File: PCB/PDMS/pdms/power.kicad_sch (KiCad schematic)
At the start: 42 parts, among them IC1 BD50FD0WHFP-TR, IC10 LDO40LPU50RY, IC11 MP2332HGTL-P, IC14 LDO40LPU50RY, IC3 LDO40LPU33RY, Q1 AO3401A, Q11 AO3401A

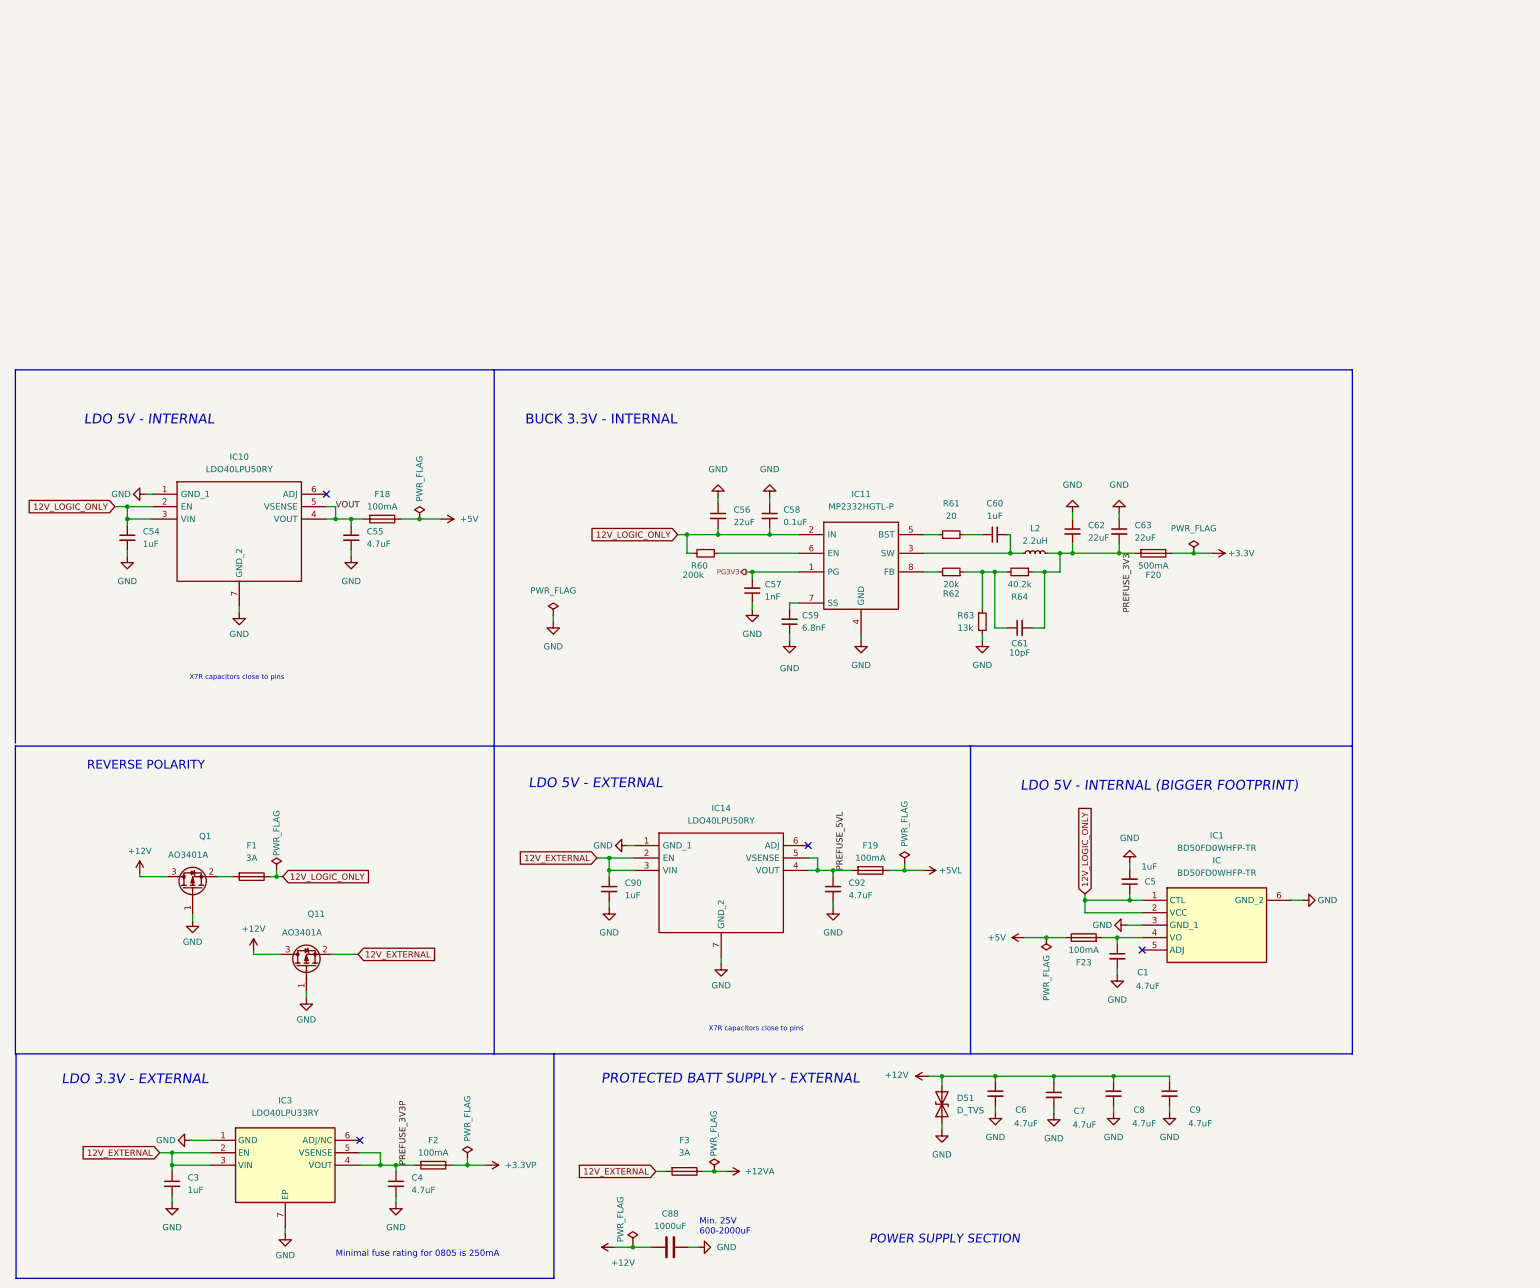
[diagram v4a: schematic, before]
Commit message: FINISHED: Version with fusing and input power filtering
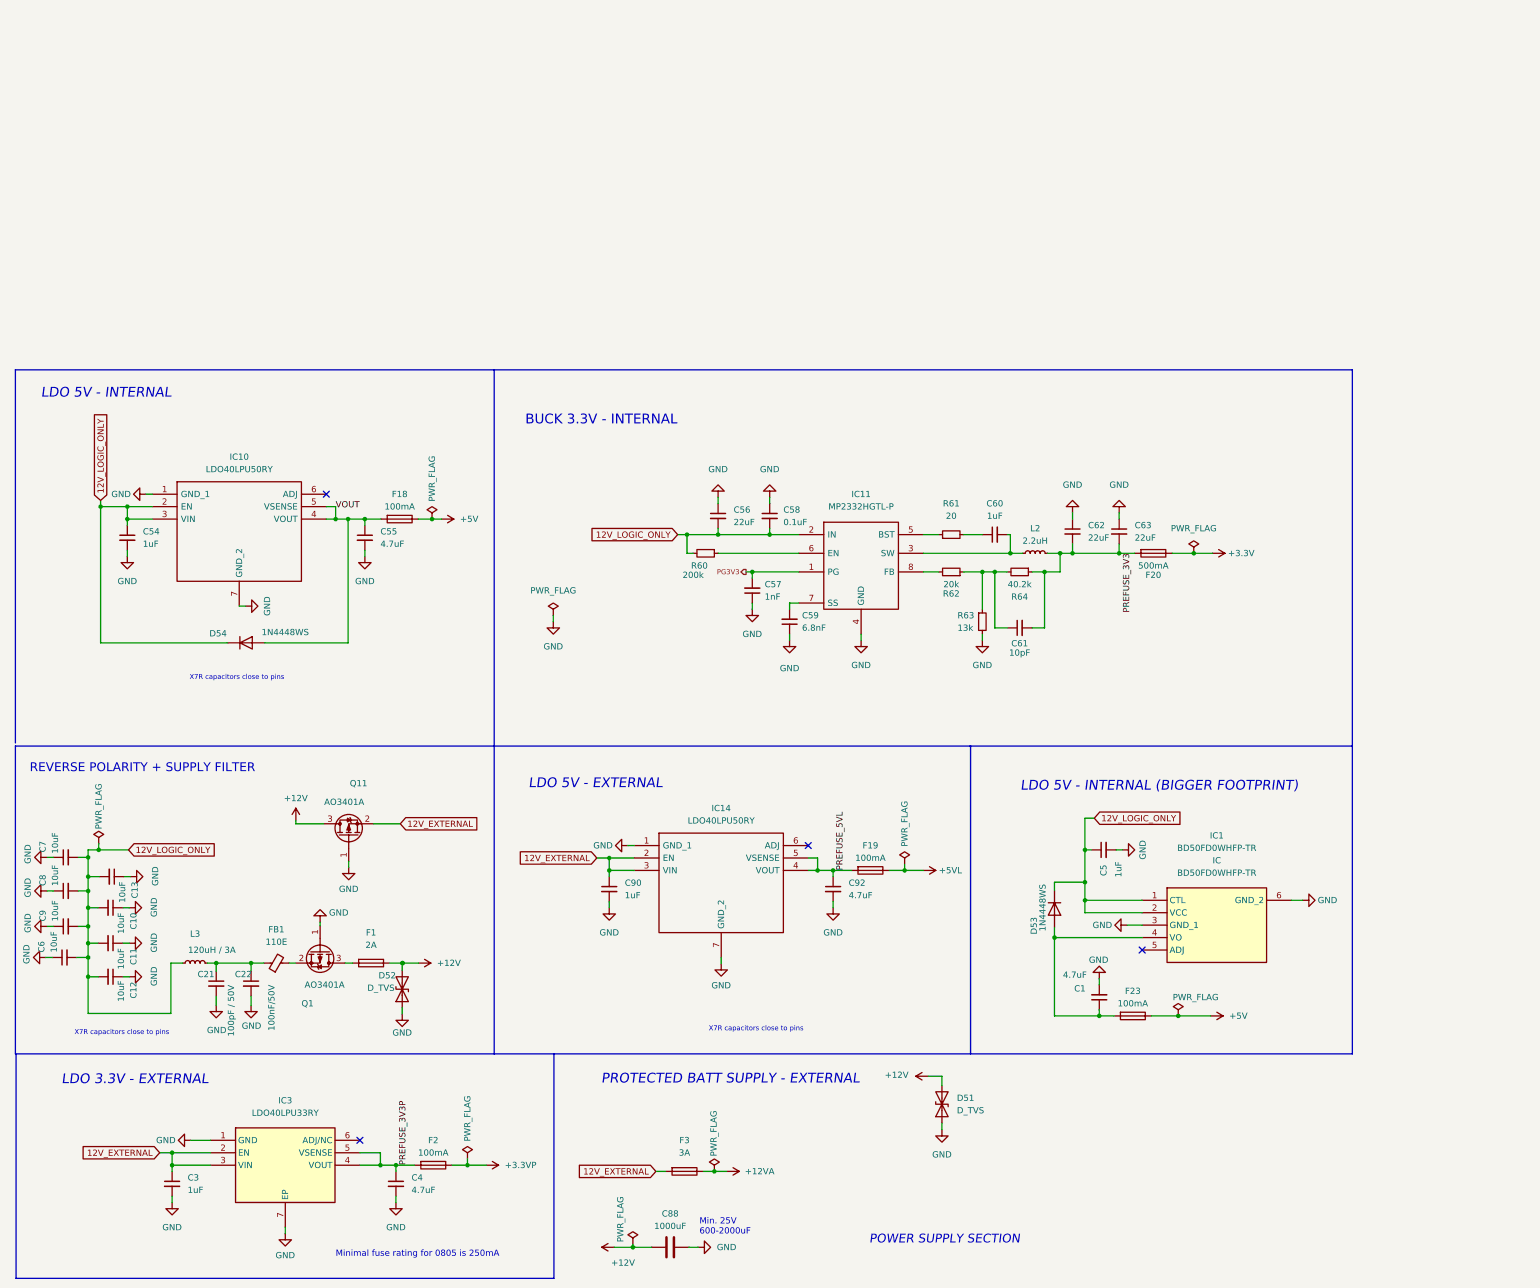
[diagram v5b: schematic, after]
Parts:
- added C10, C11, C12, C13: 10uF, Capacitor_SMD:C_1206_3216Metric, symbol Device:C_Small
- added C21: 100pF / 50V, Capacitor_SMD:C_0402_1005Metric, symbol Device:C_Small
- added C22: 100nF/50V, Capacitor_SMD:C_0402_1005Metric, symbol Device:C_Small
- added D52: D_TVS, Diode_SMD:D_SMC, symbol Device:D_TVS
- added D53, D54: 1N4448WS, Diode_SMD:D_SOD-323, symbol Diode:1N4448WS
- added FB1: 110E, Inductor_SMD:L_1206_3216Metric, symbol Device:FerriteBead_Small
- added L3: 120uH / 3A, Inductor_SMD:L_6.3x6.3_H3, symbol Device:L_Small
- C6, C7, C8, C9: value 4.7uF -> 10uF
- F1: value 3A -> 2A; footprint Fuse:Fuse_0805_2012Metric -> Fuse:Fuse_1206_3216Metric
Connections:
- net +12V: now also F1.1, D52.2 (A2); no longer C6.1, C7.1, C8.1, C9.1, Q1.3 (D)
- net 12V_LOGIC_ONLY: now also C6.2, C7.2, C8.2, C9.2, C10.2, C11.2, C12.2, C13.2, D53.1 (K), D54.1 (K), L3.1; no longer F1.1
- net GND: now also C6.1, C7.1, C8.1, C9.1, C10.1, C11.1, C12.1, C13.1, C21.2, C22.2, D52.1 (A1); no longer C6.2, C7.2, C8.2, C9.2
- net VOUT: now also D54.2 (A)
- net at C1.1, F23.2, IC1.4 (VO): now also D53.2 (A)
- net at Q1.2 (S): now also FB1.2; no longer F1.2
- new net: C21.1, C22.1, FB1.1, L3.2
- new net: F1.2, Q1.3 (D)
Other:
- note added: "REVERSE POLARITY + SUPPLY FILTER"
- note removed: "REVERSE POLARITY"
- moved on the sheet: C1, C5, C55, F1, F18, F23, Q1, Q11

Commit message: Ver 4.2 ready + BTS50025 test board
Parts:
- added C23, C24: 4.7uF, Capacitor_SMD:C_1206_3216Metric, symbol Device:C_Small
- added C25, C26: 0.1uF, Capacitor_SMD:C_0805_2012Metric, symbol Device:C_Small
- added C27: 1uF, Resistor_SMD:R_0402_1005Metric, symbol Device:C_Small
- added C28: 47nF, Resistor_SMD:R_0402_1005Metric, symbol Device:C_Small
- added C29: 10pF, Resistor_SMD:R_0402_1005Metric, symbol Device:C_Small
- added C30, C31: 22uF, Capacitor_SMD:C_1206_3216Metric, symbol Device:C_Small
- added F24: 500mA, Fuse:Fuse_0805_2012Metric, symbol Device:Fuse
- added L4: 2.2uH, Inductor_SMD:L_Vishay_IHLP-1616, symbol Device:L_Small
- added R120: 15k, Resistor_SMD:R_0402_1005Metric, symbol Device:R_Small
- added R121, R122, R124: 100k, Resistor_SMD:R_0402_1005Metric, symbol Device:R_Small
- added R123: 31.6k, Resistor_SMD:R_0402_1005Metric, symbol Device:R_Small
- added U7: MP4322GDE-P, PDMS_Additional:QFN-12_MP4322_MNP, symbol pdms_additional:MP4322GDE-P
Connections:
- net +3.3V: now also F24.1
- net 12V_LOGIC_ONLY: now also C23.1, C24.1, C25.1, C26.1, R121.1, U7.10 (VIN), U7.2 (VIN)
- net GND: now also C23.2, C24.2, C25.2, C26.2, C27.2, C30.2, C31.2, R120.1, R123.2, U7.1 (PGND), U7.11 (PGND), U7.6 (AGND)
- net PREFUSE_3V3: now also C29.2, C30.1, C31.1, F24.2, L4.2, R124.1
- new net: C29.1, R123.1, R124.2, U7.7 (FB)
- new net: R121.2, U7.9 (EN)
- new net: C28.2, L4.1, U7.12 (SW)
- new net: C28.1, U7.3 (BOOT)
- new net: R120.2, U7.4 (FREQ)
- new net: C27.1, R122.1, U7.5 (VCC)
- new net: R122.2, U7.8 (PG)
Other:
- note added: "(1206)"

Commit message: Minor changes in overall schematics & MP4322 scheamtics
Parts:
- removed C23, C24: 4.7uF, Capacitor_SMD:C_1206_3216Metric, symbol Device:C_Small
- removed C25, C26: 0.1uF, Capacitor_SMD:C_0805_2012Metric, symbol Device:C_Small
- removed C27: 1uF, Resistor_SMD:R_0402_1005Metric, symbol Device:C_Small
- removed C28: 47nF, Resistor_SMD:R_0402_1005Metric, symbol Device:C_Small
- removed C29: 10pF, Resistor_SMD:R_0402_1005Metric, symbol Device:C_Small
- removed C30, C31: 22uF, Capacitor_SMD:C_1206_3216Metric, symbol Device:C_Small
- removed F24: 500mA, Fuse:Fuse_0805_2012Metric, symbol Device:Fuse
- removed L4: 2.2uH, Inductor_SMD:L_Vishay_IHLP-1616, symbol Device:L_Small
- removed R120: 15k, Resistor_SMD:R_0402_1005Metric, symbol Device:R_Small
- removed R121, R122, R124: 100k, Resistor_SMD:R_0402_1005Metric, symbol Device:R_Small
- removed R123: 31.6k, Resistor_SMD:R_0402_1005Metric, symbol Device:R_Small
- removed U7: MP4322GDE-P, PDMS_Additional:QFN-12_MP4322_MNP, symbol pdms_additional:MP4322GDE-P
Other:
- added sheet mp4322 (mp4322.kicad_sch)
- note removed: "(1206)"

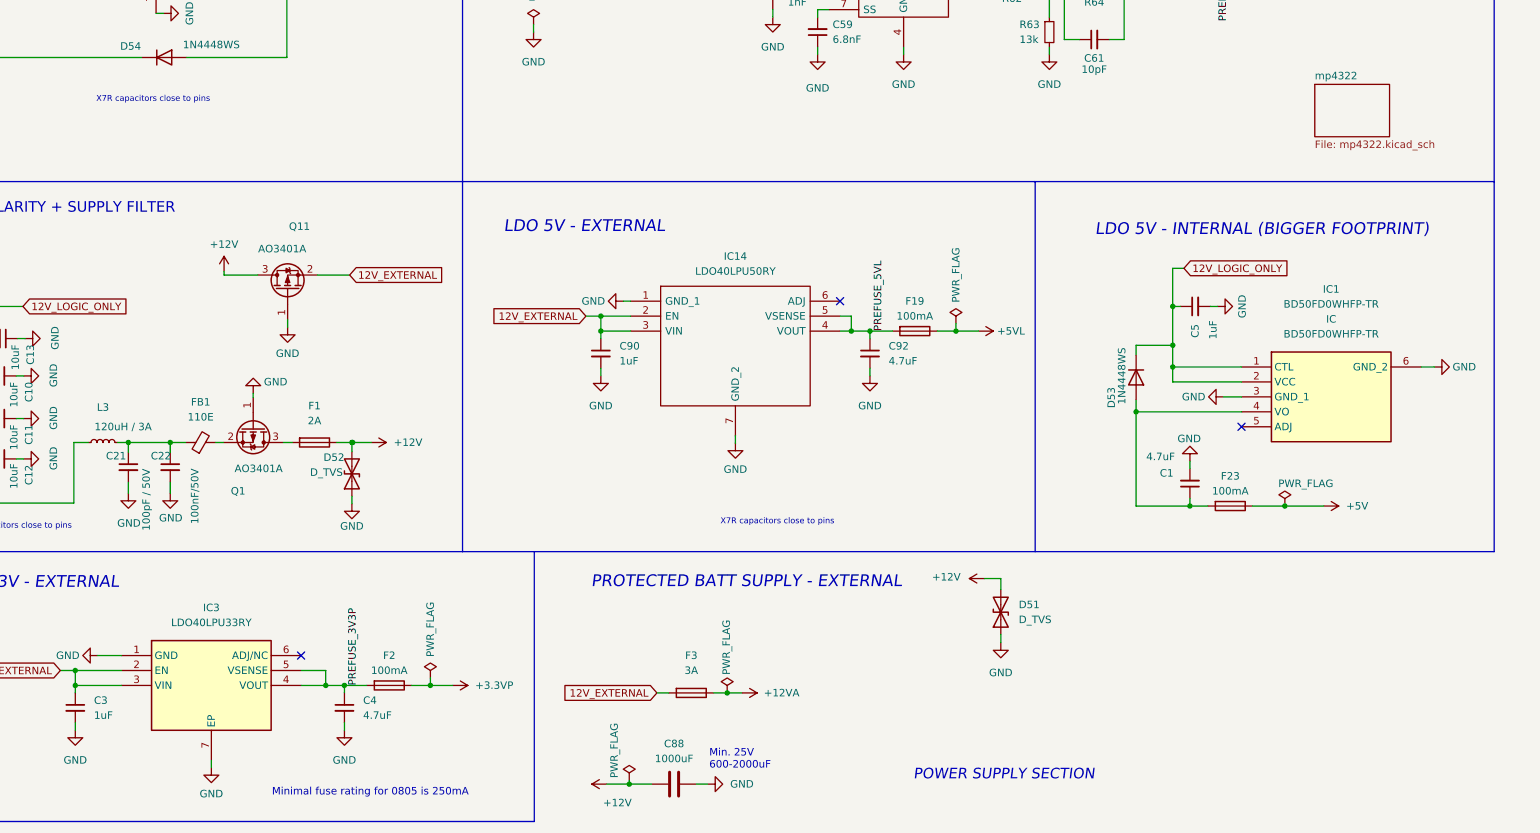
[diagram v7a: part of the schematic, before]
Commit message: WIP PCB folder structure and schematic clean-up
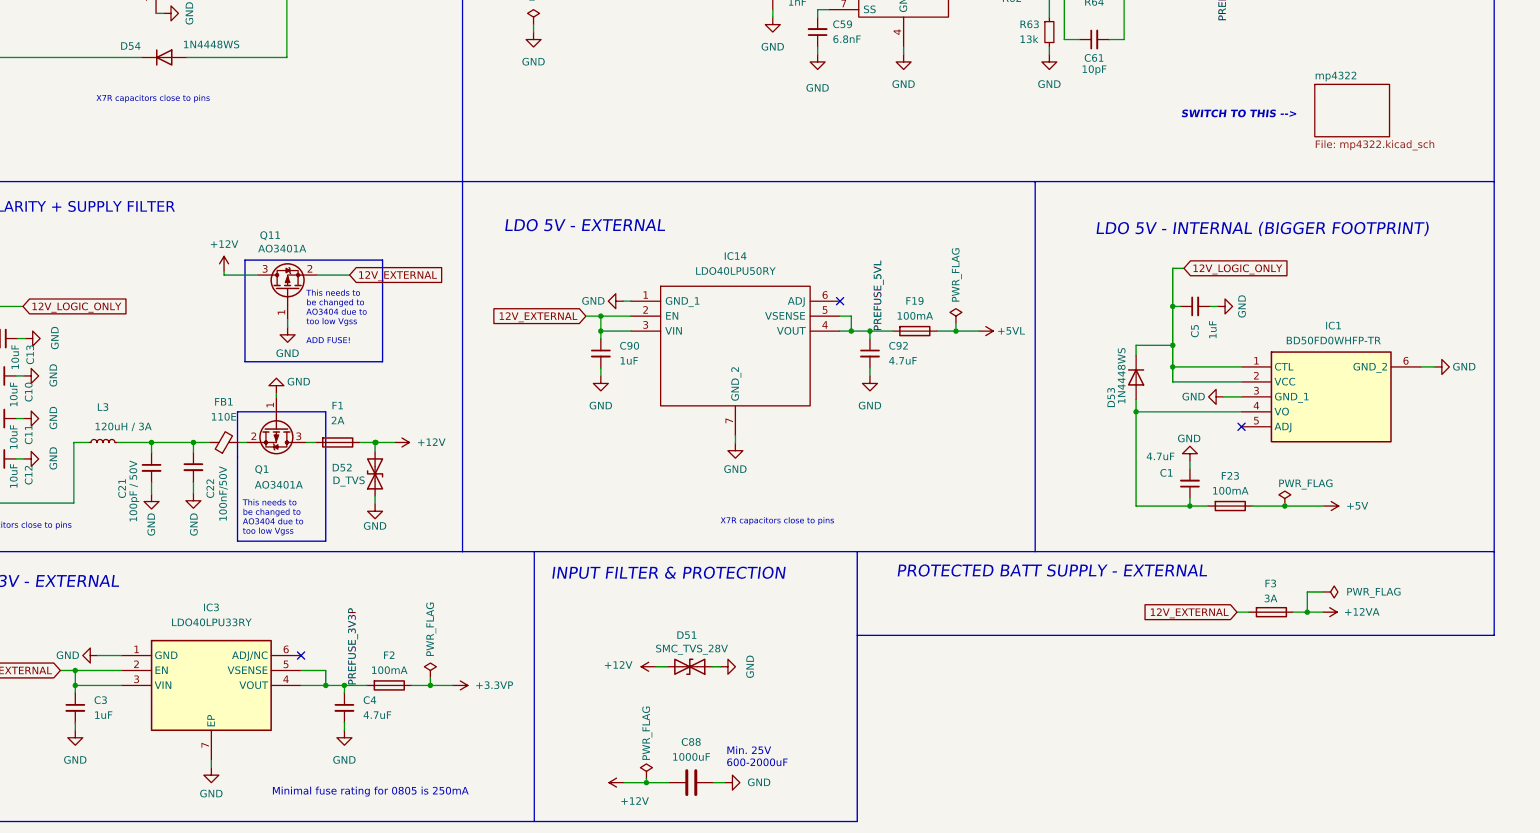
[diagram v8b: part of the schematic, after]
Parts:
- D51: value D_TVS -> SMC_TVS_28V
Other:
- note added: "INPUT FILTER & PROTECTION"
- note added: "SWITCH TO THIS -->"
- note added: "This needs to be changed to AO3404 due to too low Vgss"
- note added: "This needs to be changed to AO3404 due to too low Vgss ADD FUSE!"
- note removed: "POWER SUPPLY SECTION"
- company: (none) -> PGRacing Team
- title: (none) -> Power supply section
- moved on the sheet: C21, C22, C88, D51, D52, F1, F3, FB1, Q1
